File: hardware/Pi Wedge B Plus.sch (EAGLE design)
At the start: 14 parts

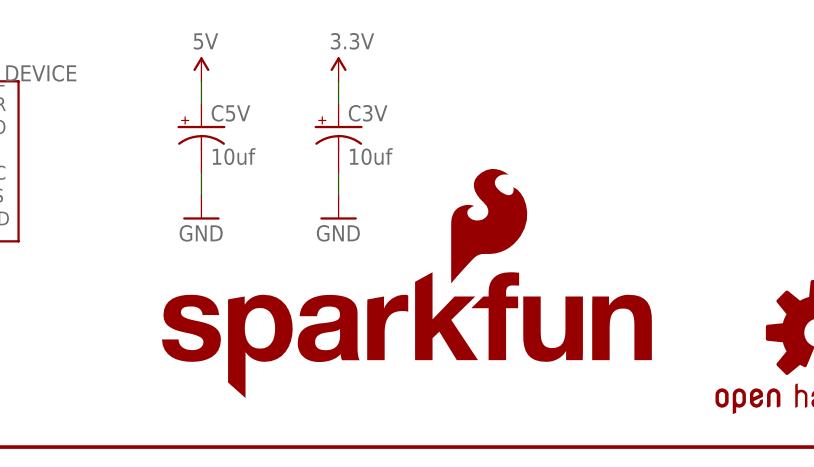
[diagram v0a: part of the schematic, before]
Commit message: Better routing.
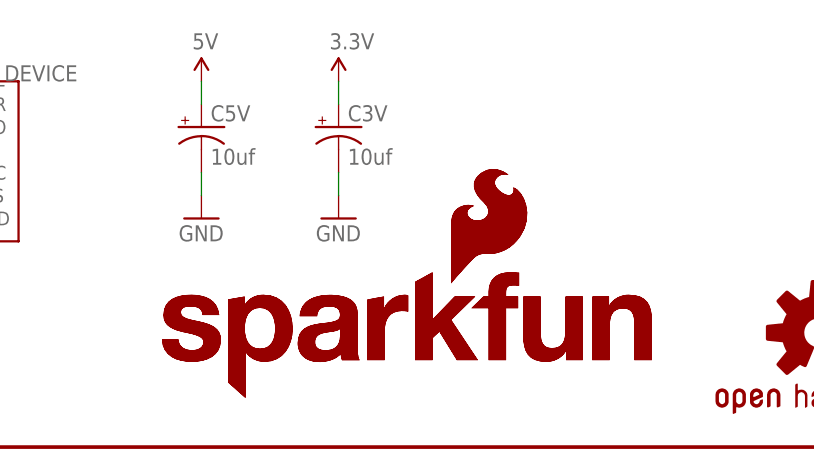
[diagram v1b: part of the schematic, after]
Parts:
- added LOGO2: SFE_LOGO_NAME_FLAME.2_INCH, SparkFun-Aesthetics:SFE_LOGO_NAME_FLAME.2_INCH
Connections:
- net N$2 renamed SCLK
- net N$3 renamed MISO
- net N$4 renamed MOSI
- net N$5 renamed CE0
- net N$6 renamed CE1
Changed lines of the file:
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@@
 <part name="SUPPLY13" library="SparkFun-Aesthetics" deviceset="5V" device=""/>
 <part name="SUPPLY14" library="SparkFun-Aesthetics" deviceset="3.3V" device=""/>
+<part name="LOGO2" library="SparkFun-Aesthetics" deviceset="SFE_LOGO_NAME_FLAME" device=".2_INCH"/>
 </parts>
 <sheets>
@@
 <instance part="SUPPLY13" gate="G$1" x="71.12" y="139.7"/>
 <instance part="SUPPLY14" gate="G$1" x="60.96" y="139.7"/>
+<instance part="LOGO2" gate="G$1" x="55.88" y="5.08"/>
 </instances>
 <busses>
@@
 </segment>
 </net>
-<net name="N$2" class="0">
+<net name="SCLK" class="0">
 <segment>
 <pinref part="U$3" gate="G$1" pin="SCLK"/>
@@
 </segment>
 </net>
-<net name="N$3" class="0">
+<net name="MISO" class="0">
 <segment>
 <pinref part="U$3" gate="G$1" pin="MISO"/>
@@
 </segment>
 </net>
-<net name="N$4" class="0">
+<net name="MOSI" class="0">
 <segment>
 <pinref part="U$3" gate="G$1" pin="MOSI"/>
@@
 </segment>
 </net>
-<net name="N$5" class="0">
+<net name="CE0" class="0">
 <segment>
 <pinref part="U$3" gate="G$1" pin="CE0"/>
@@
 </segment>
 </net>
-<net name="N$6" class="0">
+<net name="CE1" class="0">
 <segment>
 <pinref part="U$3" gate="G$1" pin="CE1"/>

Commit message: Bumping rev number for reds
From V01 to V10.
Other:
- note added: "V10"
- note removed: "V01"
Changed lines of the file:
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@@
 <plain>
 <text x="167.64" y="10.16" size="2.54" layer="94">Byron Jacquot</text>
-<text x="238.76" y="7.62" size="2.54" layer="94">V01</text>
+<text x="238.76" y="7.62" size="2.54" layer="94">V10</text>
 </plain>
 <instances>

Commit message: Review updates
Based on Pete Lewis's comments.
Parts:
- removed JP5: LOGO-SFESK, SparkFun:LOGO-SFESK
- removed U$1: OSHW-LOGOS, SparkFun:OSHW-LOGOS
- removed U$5: M17KIT, SparkFun-Connectors:M17KIT
- added LOGO3, LOGO4: SFE_LOGO_FLAME.1_INCH, SparkFun-Aesthetics:SFE_LOGO_FLAME.1_INCH
- added LOGO5: OSHW-LOGOS, SparkFun-Aesthetics:OSHW-LOGOS
- JP1: value LOGO-SFESK -> FTDI_DEVICE; device SparkFun:LOGO-SFESK -> SparkFun-Connectors:FTDI_DEVICE
- JP4: value FTDI_DEVICE -> M17KIT; device SparkFun-Connectors:FTDI_DEVICE -> SparkFun-Connectors:M17KIT
- renumbered U$3 to JP2, U$4 to JP3
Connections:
- net 3.3V: now also JP4.2; no longer U$5.2
- net 5V: now also JP4.3; no longer U$5.3
- net GND: now also JP1.GND, JP4.1; no longer JP4.GND, U$5.1
- net GP18: now also JP4.17; no longer U$5.17
- net GP19: now also JP4.16; no longer U$5.16
- net GP20: now also JP4.15; no longer U$5.15
- net GP21: now also JP4.14; no longer U$5.14
- net GP22: now also JP4.13; no longer U$5.13
- net GP23: now also JP4.12; no longer U$5.12
- net GP24: now also JP4.11; no longer U$5.11
- net GP25: now also JP4.10; no longer U$5.10
- net GP26: now also JP4.9; no longer U$5.9
- net GP27: now also JP4.8; no longer U$5.8
- net ID_SC: now also JP4.5; no longer U$5.5
- net ID_SD: now also JP4.4; no longer U$5.4
- net RXI: now also JP1.RXI; no longer JP4.RXI
- net SCL: now also JP4.7; no longer U$5.7
- net SDA: now also JP4.6; no longer U$5.6
- net TXO: now also JP1.TXO; no longer JP4.TXO
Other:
- note added: "All logic signals are 3.3V, and not 5V tolerant. There is no over-voltage protection on the RPi, nor on the Pi Wedge B+."
- note added: "TXO and RXI use 3.3V logic levels. Use with 3.3V FTDI adapter."
- note added: "V11"
- note removed: "V10"
